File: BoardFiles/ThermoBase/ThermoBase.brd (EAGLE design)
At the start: 100 x 96.5 mm, 31 parts, among them CON1 BARREL_JACK_3PIN, U1 MOSFET_N, U2 MOSFET_N, U3 MOSFET_N, U4 LM317

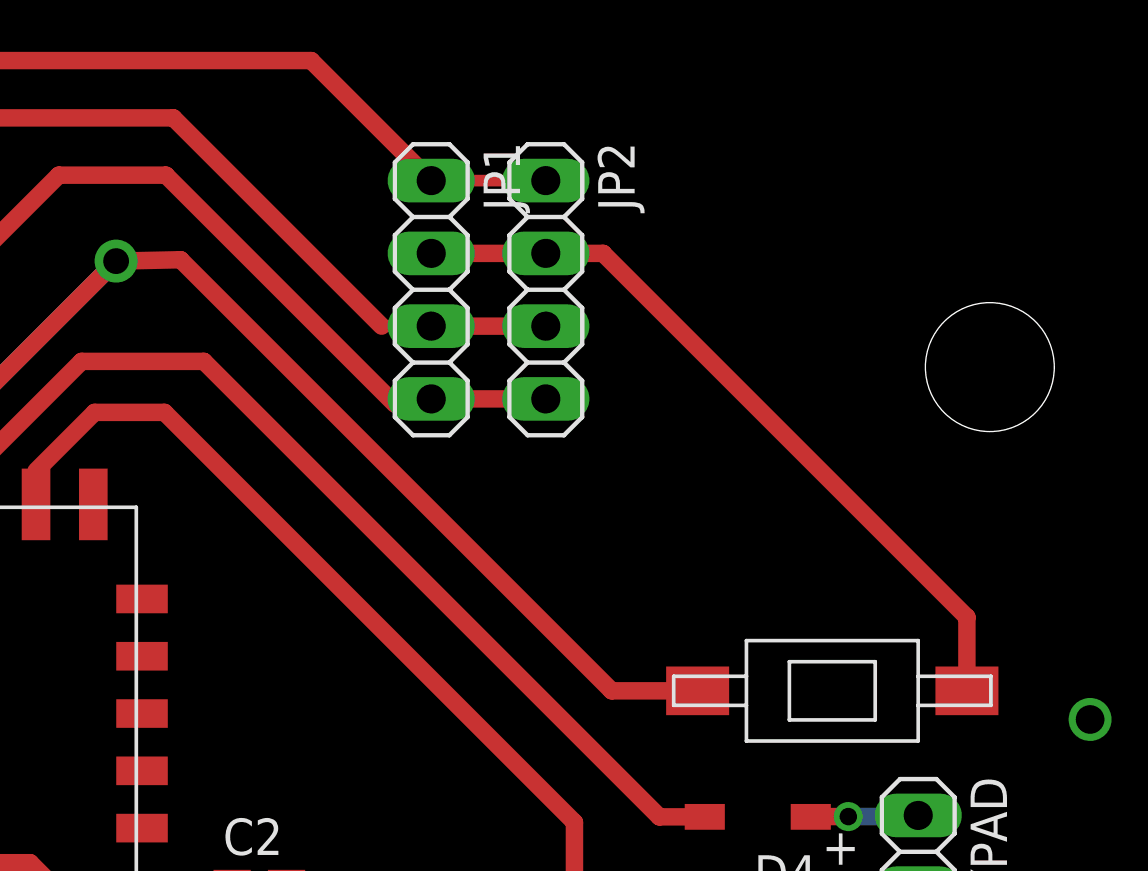
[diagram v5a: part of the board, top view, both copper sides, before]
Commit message: Found some board errors and got an AC demo ready
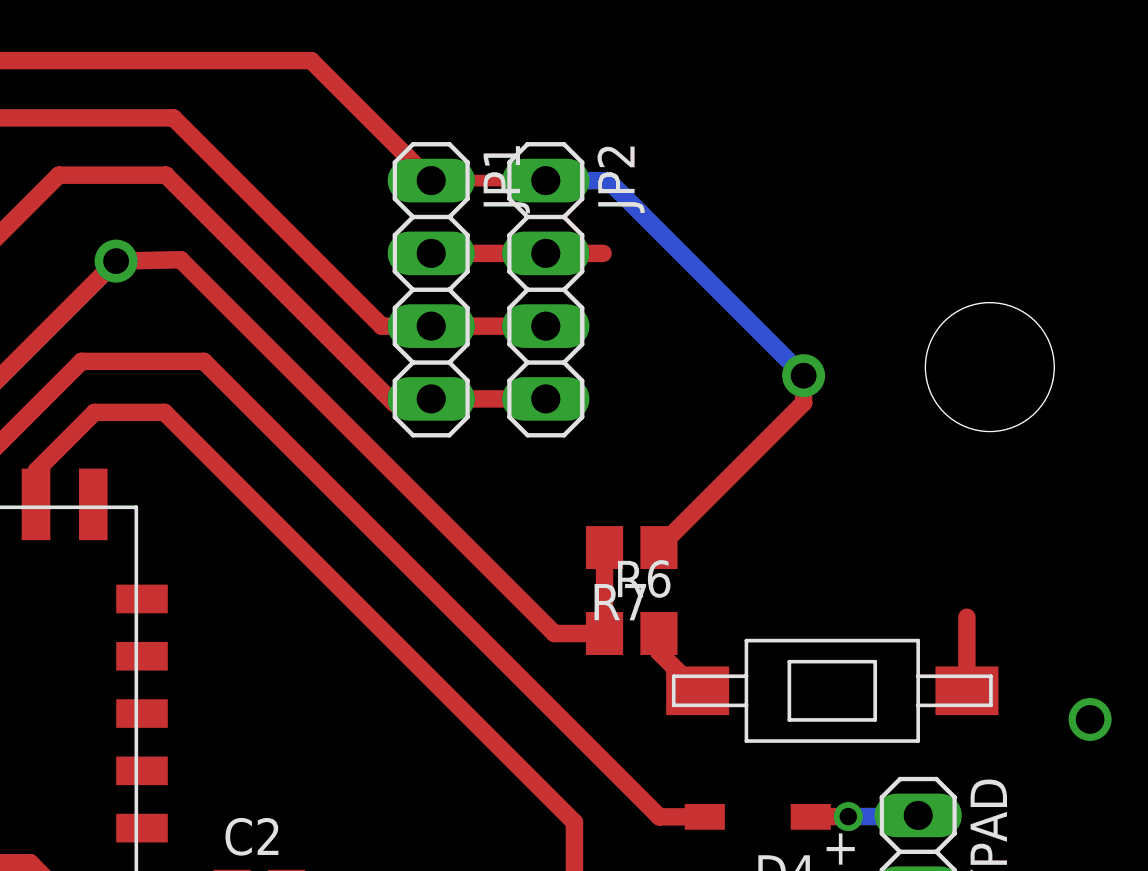
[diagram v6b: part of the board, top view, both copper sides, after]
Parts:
- added R6: 1K, DR:R0805
- added R7: 10K, DR:R0805
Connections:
- new net N$16: BTN1.1, R6.2
- net +3V3: now also R7.1
- net LCDE: now also R6.1, R7.2; no longer BTN1.1
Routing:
- net +3V3: track 200.5 -> 220.4 mm, vias 1 -> 2
- net GND: track 66.2 -> 48.3 mm
- net N$16: track 0.00 -> 2.56 mm
- net LCDE: track 99.7 -> 98.6 mm
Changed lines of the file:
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@@
 <attribute name="VALUE" x="74.825" y="87.08" size="1.27" layer="27" rot="R270"/>
+</element>
+<element name="R6" library="DR" package="R0805" value="1K" x="81" y="70" smashed="yes">
+<attribute name="NAME" x="80.365" y="71.27" size="1.27" layer="25"/>
+<attribute name="VALUE" x="80.365" y="67.46" size="1.27" layer="27"/>
+</element>
+<element name="R7" library="DR" package="R0805" value="10K" x="81" y="73" smashed="yes" rot="R180">
+<attribute name="NAME" x="81.635" y="71.73" size="1.27" layer="25" rot="R180"/>
+<attribute name="VALUE" x="81.635" y="75.54" size="1.27" layer="27" rot="R180"/>
 </element>
 </elements>
@@
 <contactref element="JP2" pad="2"/>
 <wire x1="78" y1="83.27" x2="74" y2="83.27" width="0.6096" layer="1"/>
-<wire x1="92.7" y1="70.57" x2="80" y2="83.27" width="0.6096" layer="1"/>
 <wire x1="78" y1="83.27" x2="80" y2="83.27" width="0.6096" layer="1"/>
 <wire x1="92.7" y1="70.57" x2="92.7" y2="68" width="0.6096" layer="1"/>
@@
 <wire x1="45.415" y1="48.415" x2="41.535" y2="48.415" width="0.6096" layer="1"/>
 <via x="41.46" y="48.43" extent="1-16" drill="0.9" diameter="1.5"/>
-<wire x1="74" y1="83.27" x2="62.205" y2="74.507" width="0" layer="19" extent="1-1"/>
 </signal>
 <signal name="N$1">
@@
 <wire x1="69.81" y1="90" x2="45" y2="90" width="0.6096" layer="1"/>
 <wire x1="74" y1="85.81" x2="78" y2="85.81" width="0.4064" layer="1"/>
+<contactref element="R7" pad="1"/>
+<wire x1="81.95" y1="73" x2="87" y2="78.05" width="0.6096" layer="1"/>
+<wire x1="87" y1="78.05" x2="87" y2="79" width="0.6096" layer="1"/>
+<via x="87" y="79" extent="1-16" drill="0.9" diameter="1.5"/>
+<wire x1="87" y1="79" x2="80.19" y2="85.81" width="0.6096" layer="16"/>
+<wire x1="80.19" y1="85.81" x2="78" y2="85.81" width="0.6096" layer="16"/>
 </signal>
 <signal name="SDA">
@@
 <contactref element="JP1" pad="3"/>
 <contactref element="JP2" pad="3"/>
-<wire x1="74" y1="80.73" x2="72.27" y2="80.73" width="0.4064" layer="1"/>
+<wire x1="74" y1="80.73" x2="72.27" y2="80.73" width="0.6096" layer="1"/>
 <wire x1="65" y1="88" x2="57" y2="88" width="0.6096" layer="1"/>
 <via x="57" y="88" extent="1-16" drill="0.9" diameter="1.5"/>
@@
 <signal name="LCDE">
 <contactref element="JP3" pad="1"/>
-<contactref element="BTN1" pad="1"/>
 <contactref element="U$1" pad="12"/>
 <wire x1="56.205" y1="74.507" x2="56.205" y2="76.205" width="0.6096" layer="1"/>
@@
 <via x="63" y="83" extent="1-16" drill="0.9" diameter="1.5"/>
 <wire x1="65.25175" y1="83.04825" x2="63" y2="83" width="0.6096" layer="1"/>
-<wire x1="80.3" y1="68" x2="65.25175" y2="83.04825" width="0.6096" layer="1"/>
-<wire x1="80.3" y1="68" x2="83.3" y2="68" width="0.6096" layer="1"/>
+<wire x1="78.3" y1="70" x2="65.25175" y2="83.04825" width="0.6096" layer="1"/>
 <wire x1="8.73" y1="68.73" x2="15" y2="75" width="0.6096" layer="16"/>
 <wire x1="15" y1="75" x2="55" y2="75" width="0.6096" layer="16"/>
 <wire x1="55" y1="75" x2="63" y2="83" width="0.6096" layer="16"/>
+<contactref element="R6" pad="1"/>
+<contactref element="R7" pad="2"/>
+<wire x1="80.05" y1="70" x2="78.3" y2="70" width="0.6096" layer="1"/>
+<wire x1="80.05" y1="70" x2="80.05" y2="73" width="0.6096" layer="1"/>
 </signal>
 <signal name="N$11">
@@
 <wire x1="87.3025" y1="53.4675" x2="87.255" y2="53.515" width="0.6096" layer="1"/>
 </signal>
+<signal name="N$16">
+<contactref element="BTN1" pad="1"/>
+<contactref element="R6" pad="2"/>
+<wire x1="83.3" y1="68" x2="81.95" y2="69.35" width="0.6096" layer="1"/>
+<wire x1="81.95" y1="69.35" x2="81.95" y2="70" width="0.6096" layer="1"/>
+</signal>
 </signals>

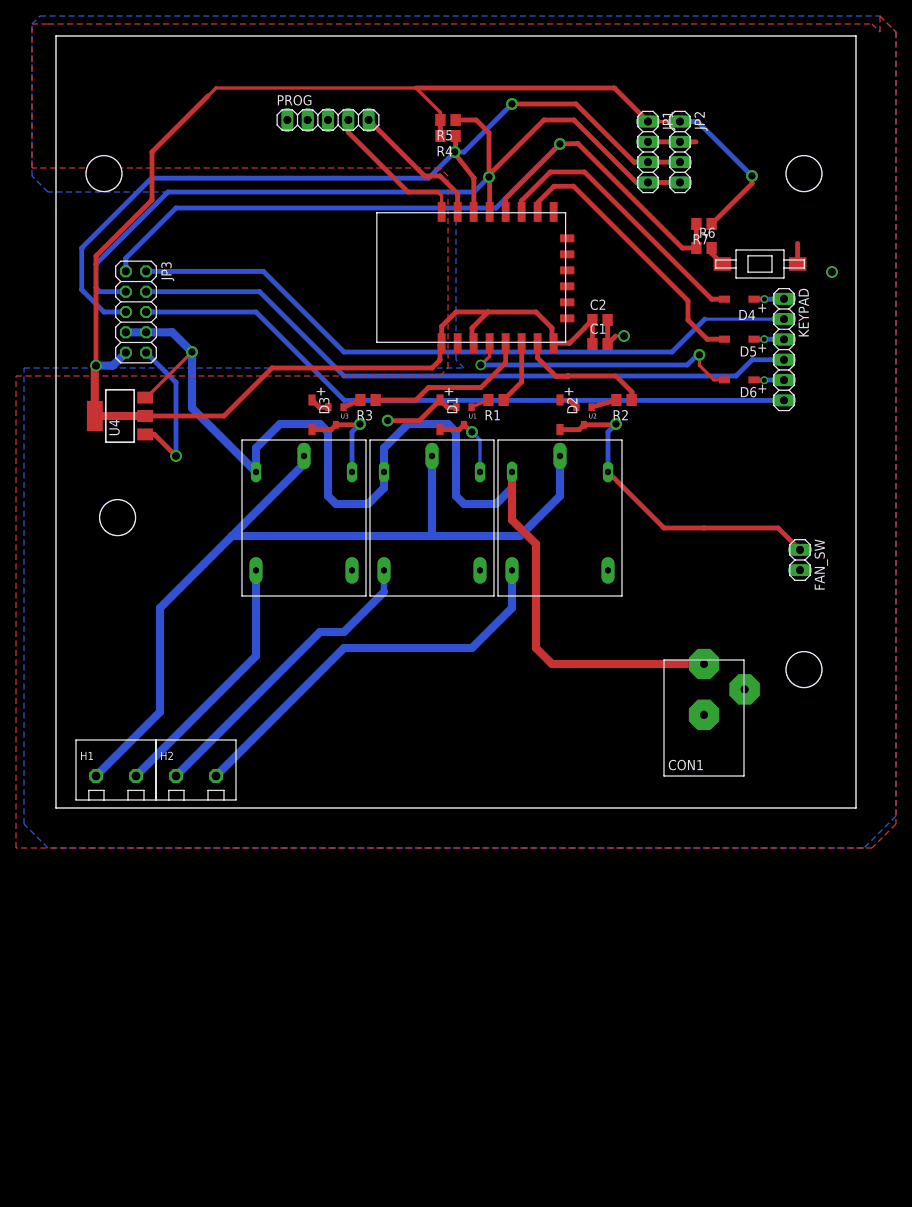
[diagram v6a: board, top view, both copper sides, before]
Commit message: Ordered boards V1.0
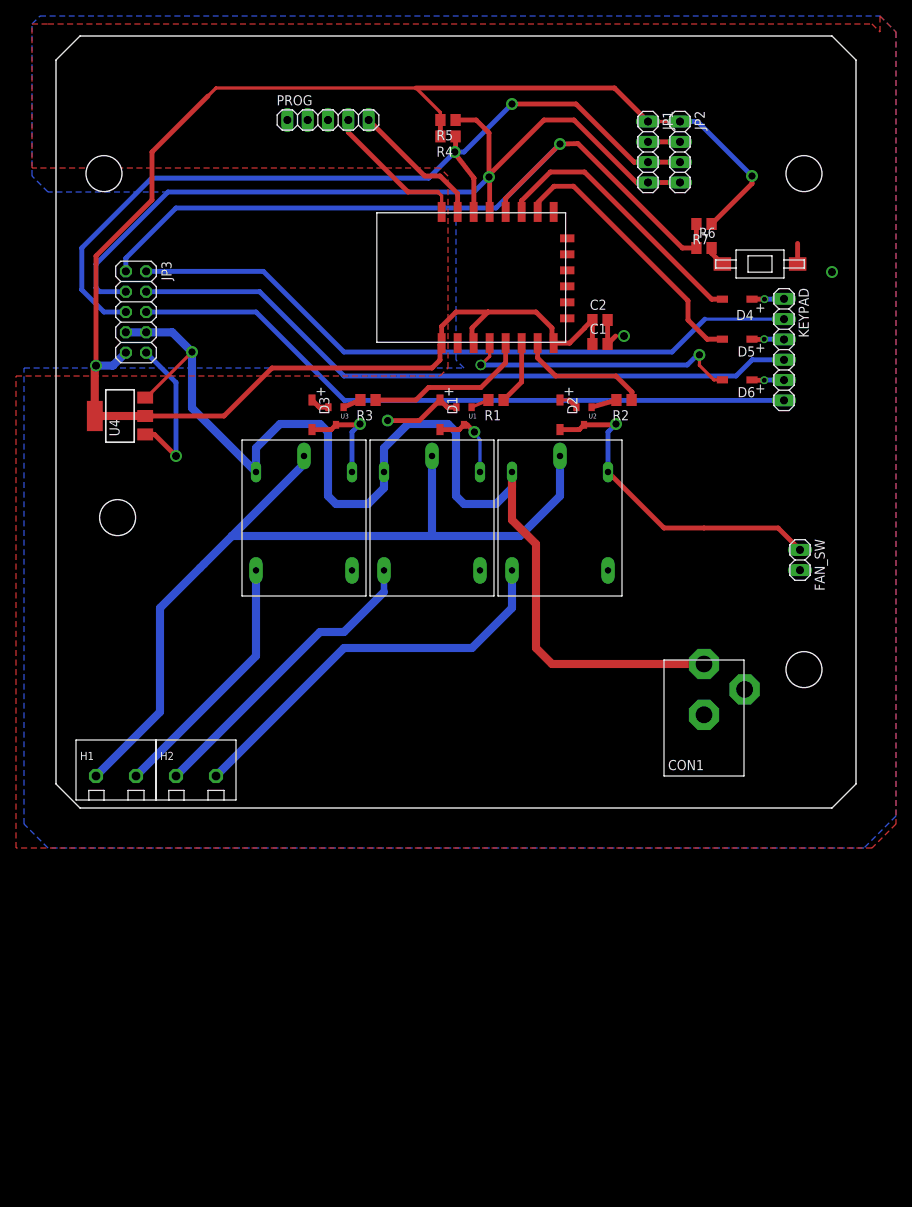
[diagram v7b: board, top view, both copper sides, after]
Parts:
- CON1: value BARREL_JACK_3PIN -> BARREL_JACK_3PINPJ-102A_2MM_HOLES; device DR:PJ-102A -> DR:PJ-102A_2MM_HOLES
- moved D6 0.25 mm to (87.0, 53.5)
- moved D4 0.25 mm to (87.0, 63.6)
- moved D5 0.25 mm to (87.0, 58.6)
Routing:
- net GND: track 48.3 -> 46.3 mm
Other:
- outline, holes or cut-outs redrawn
- board text added: "ESP12 Thermo Board V1.0 6/6/25"
